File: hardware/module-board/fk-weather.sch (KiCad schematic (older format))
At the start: 71 parts, among them J1 MICRO-USB, J10 Conn_01x06, J11 Conn_01x06, J2 Conn_01x05, J3 CONN_01x03_SERIAL, J4 CONN_01x04, J5 Conn_01x02, J6 CONN_02x05_SWD, J7 Conn_01x05, M1 MOUNT_HOLE, M2 MOUNT_HOLE, M3 MOUNT_HOLE, M4 MOUNT_HOLE, Q4 2N7002LT1G, SW1 SPNO, U1 ATSAMD21G18A-AU, U2 MCP1700T-3302E/MB, U3 TPS2051B, U4 S25FL116K0XMFI041, U5 SK6812, U6 PCF8523, Y1 FC-135, Y2 FC-135

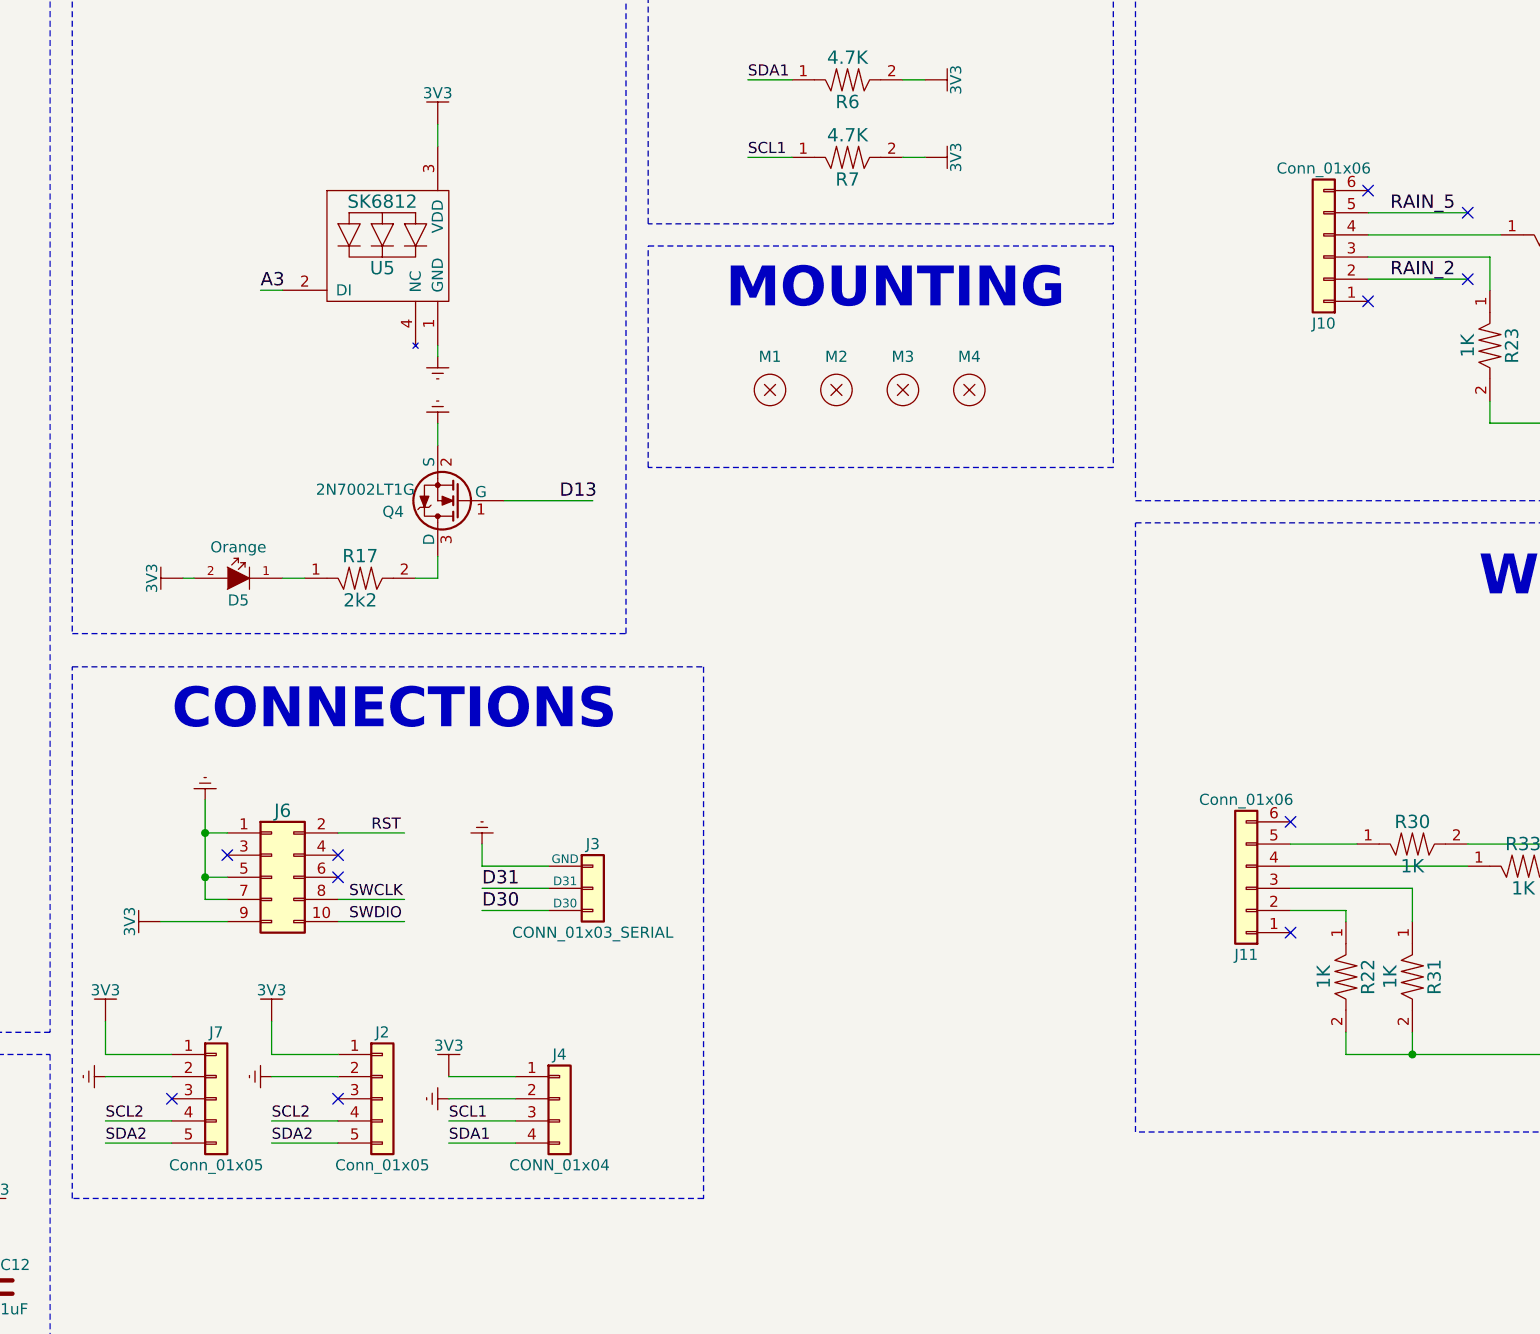
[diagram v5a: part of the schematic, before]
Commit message: Schematic/FP cleanup. Nothing major.
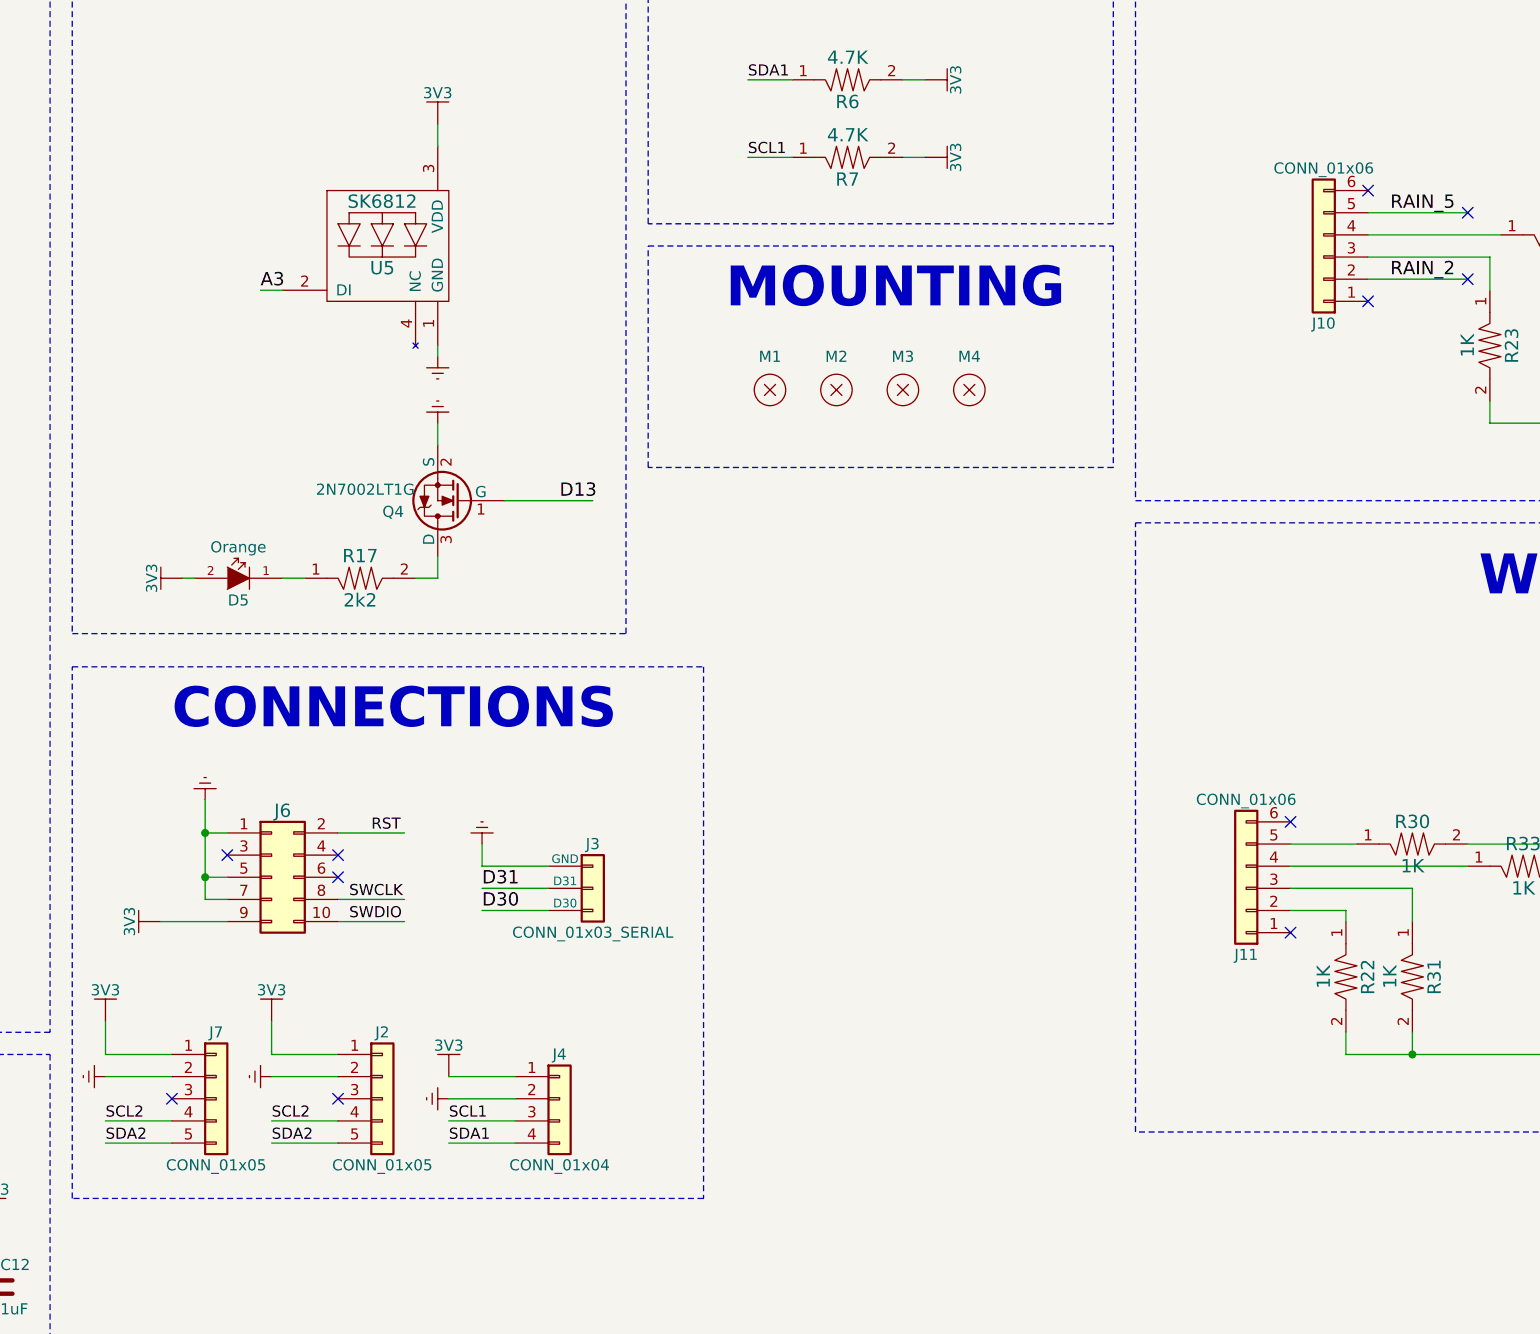
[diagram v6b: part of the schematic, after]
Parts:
- J10, J11: value Conn_01x06 -> CONN_01x06; footprint conservify:wurth_615006138421 -> conservify:WURTH_615006138421
- J2, J7: value Conn_01x05 -> CONN_01x05
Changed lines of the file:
@@
 P 12600 4900
 F 0 "J11" H 12600 5200 50  0000 C CNN
-F 1 "Conn_01x06" H 12600 4500 50  0000 C CNN
-F 2 "conservify:wurth_615006138421" H 12600 4900 50  0001 C CNN
+F 1 "CONN_01x06" H 12600 4500 50  0000 C CNN
+F 2 "conservify:WURTH_615006138421" H 12600 4900 50  0001 C CNN
 F 3 "" H 12600 4900 50  0001 C CNN
 F 4 " " H 12600 5300 50  0001 C CNN "Critical"
@@
 P 12950 2050
 F 0 "J10" H 12950 2350 50  0000 C CNN
-F 1 "Conn_01x06" H 12950 1650 50  0000 C CNN
-F 2 "conservify:wurth_615006138421" H 12950 2050 50  0001 C CNN
+F 1 "CONN_01x06" H 12950 1650 50  0000 C CNN
+F 2 "conservify:WURTH_615006138421" H 12950 2050 50  0001 C CNN
 F 3 "" H 12950 2050 50  0001 C CNN
 F 4 " " H 12950 2450 50  0001 C CNN "Critical"
@@
 P 8700 5850
 F 0 "J2" H 8700 6150 50  0000 C CNN
-F 1 "Conn_01x05" H 8700 5550 50  0000 C CNN
+F 1 "CONN_01x05" H 8700 5550 50  0000 C CNN
 F 2 "conservify:Molex_CLIK-Mate_502382-0570_1x05_P1.25mm_Vertical" H 8700 5850 50  0001 C CNN
 F 3 "" H 8700 5850 50  0001 C CNN
@@
 P 7950 5850
 F 0 "J7" H 7950 6150 50  0000 C CNN
-F 1 "Conn_01x05" H 7950 5550 50  0000 C CNN
+F 1 "CONN_01x05" H 7950 5550 50  0000 C CNN
 F 2 "conservify:Molex_CLIK-Mate_502382-0570_1x05_P1.25mm_Vertical" H 7950 5850 50  0001 C CNN
 F 3 "" H 7950 5850 50  0001 C CNN

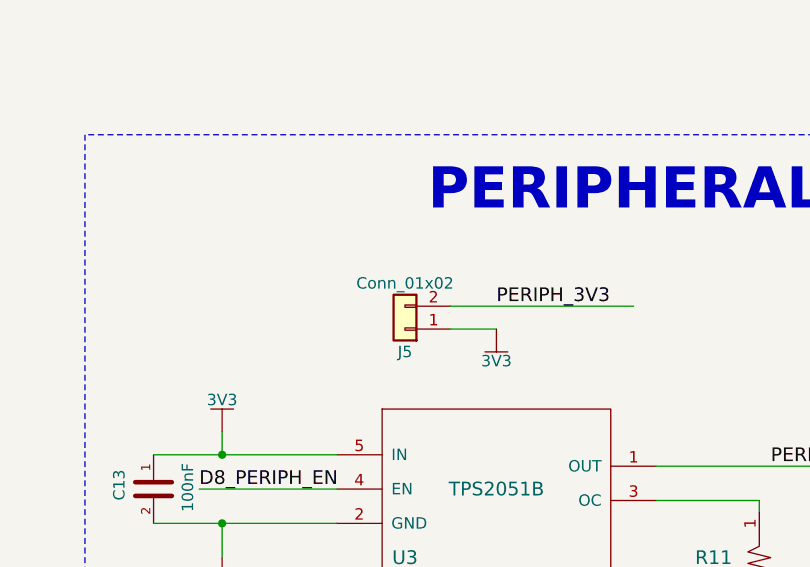
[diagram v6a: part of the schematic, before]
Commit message: Consistency in part values
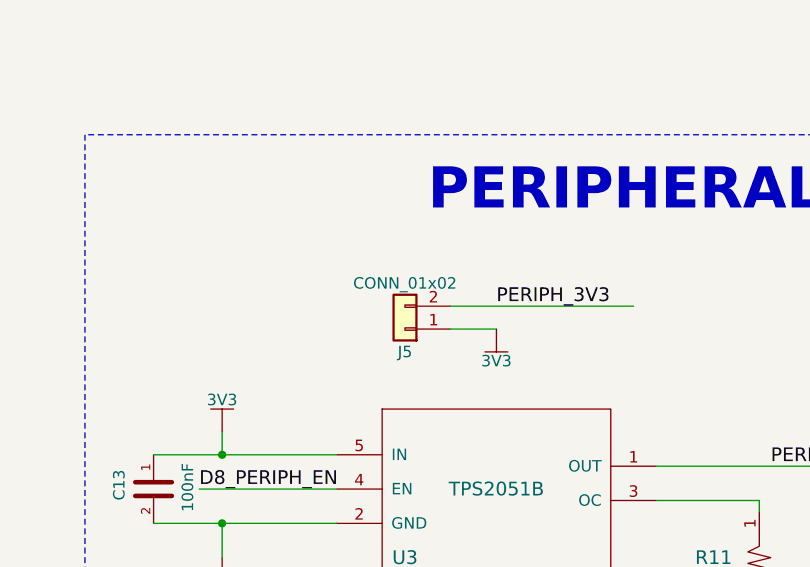
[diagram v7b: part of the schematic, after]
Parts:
- J10, J11: MFN (none) -> Wurth Electronics; MFP (none) -> 615006138421; SPN1 (none) -> 732-2113-ND; Supplier1 (none) -> digikey
- J4: MFN (none) -> Molex; MFP (none) -> 502382-0470; SPN1 (none) -> WM4781CT-ND; Supplier1 (none) -> digikey
- J5: value Conn_01x02 -> CONN_01x02
- U3: MFN (none) -> Texas Instruments; MFP (none) -> TPS2051BDBVR; SPN1 (none) -> 296-21265-1-ND; Supplier1 (none) -> digikey

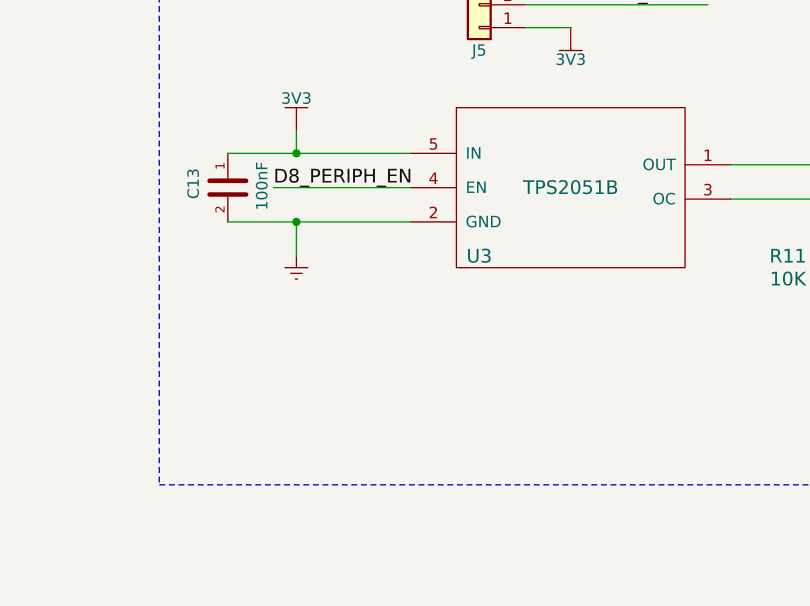
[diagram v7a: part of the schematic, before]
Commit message: Adding some pull downs.
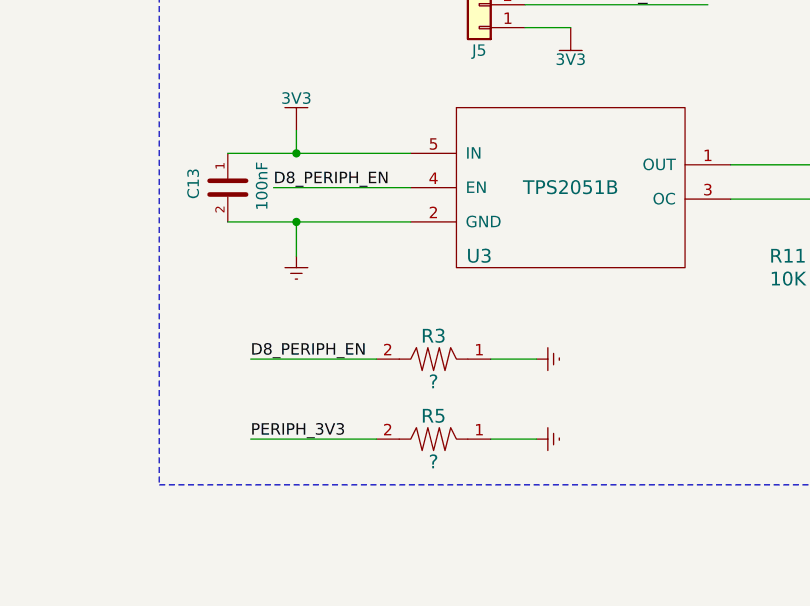
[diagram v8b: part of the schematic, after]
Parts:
- added R3, R5: ?, conservify:RES-0603, symbol conservify:RESISTOR
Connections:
- wire segments 287 -> 291
